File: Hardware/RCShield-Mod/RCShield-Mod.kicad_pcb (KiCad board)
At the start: 2 copper layers, 12 parts, among them K1 PPM_OUT, P1 ANALOG_EXT, P2 DIGI_EXT, P7 Vinput

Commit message: Changing VIA Size for the Analog Board Moving Analog Board away from Digital board connector
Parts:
- moved P1 9.40 mm to (109.0, 88.1)
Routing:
- net SCL: track 46.6 -> 55.9 mm
- net SDA: track 52.7 -> 59.9 mm
- net +5V: track 59.6 -> 57.0 mm
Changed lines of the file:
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@@
     (links 45)
     (no_connects 0)
-    (area 0 0 0 0)
+    (area 61.611934 74.676 167.640001 167.580733)
     (thickness 1.6)
     (drawings 0)
-    (tracks 123)
+    (tracks 121)
     (zones 0)
     (modules 12)
@@
   )
   (module PIN_ARRAY_4x1 (layer F.Cu)
-    (at 118.364 88.138)
+    (at 108.966 88.138)
     (descr "Double rangee de contacts 2 x 5 pins")
     (tags CONN)
@@
     )
   )
-  (segment (start 131.572 78.867) (end 136.779 78.867) (width 0.254) (layer F.Cu) (net 1))
-  (segment (start 114.554 86.106) (end 120.142 80.518) (width 0.254) (layer F.Cu) (net 1))
-  (segment (start 120.142 80.518) (end 138.43 80.518) (width 0.254) (layer F.Cu) (net 1))
-  (via (at 138.43 80.518) (size 2) (layers F.Cu B.Cu) (net 1))
-  (segment (start 114.554 86.106) (end 114.554 88.138) (width 0.254) (layer F.Cu) (net 1))
-  (segment (start 136.779 78.867) (end 138.43 80.518) (width 0.254) (layer F.Cu) (net 1))
+  (segment (start 131.572 78.867) (end 120.777 78.867) (width 0.254) (layer F.Cu) (net 1) (status 400000))
+  (segment (start 105.156 83.312) (end 109.474 78.994) (width 0.254) (layer F.Cu) (net 1))
+  (segment (start 109.474 78.994) (end 120.65 78.994) (width 0.254) (layer F.Cu) (net 1))
+  (via (at 120.65 78.994) (size 2) (layers F.Cu B.Cu) (net 1))
+  (segment (start 105.156 83.312) (end 105.156 88.138) (width 0.254) (layer F.Cu) (net 1) (status 800000))
+  (segment (start 120.777 78.867) (end 120.65 78.994) (width 0.254) (layer F.Cu) (net 1))
   (segment (start 145.288 88.138) (end 138.43 88.138) (width 0.254) (layer F.Cu) (net 1))
   (segment (start 138.303 88.265) (end 138.43 88.138) (width 0.254) (layer F.Cu) (net 1))
@@
   (segment (start 104.394 136.906) (end 108.204 136.906) (width 0.254) (layer B.Cu) (net 14))
   (segment (start 107.696 136.906) (end 108.204 136.906) (width 0.254) (layer B.Cu) (net 14))
-  (segment (start 131.572 82.169) (end 122.555 82.169) (width 0.254) (layer F.Cu) (net 15))
-  (segment (start 119.634 85.09) (end 119.634 88.138) (width 0.254) (layer F.Cu) (net 15))
-  (segment (start 122.555 82.169) (end 119.634 85.09) (width 0.254) (layer F.Cu) (net 15))
+  (segment (start 110.236 88.138) (end 110.236 85.344) (width 0.254) (layer F.Cu) (net 15) (status 400000))
+  (segment (start 113.411 82.169) (end 131.572 82.169) (width 0.254) (layer F.Cu) (net 15) (status 800000))
+  (segment (start 110.236 85.344) (end 113.411 82.169) (width 0.254) (layer F.Cu) (net 15))
   (segment (start 135.382 82.296) (end 131.699 82.296) (width 0.254) (layer F.Cu) (net 15))
   (segment (start 150.368 86.36) (end 146.304 82.296) (width 0.254) (layer F.Cu) (net 15))
@@
   (segment (start 131.699 82.296) (end 131.572 82.169) (width 0.254) (layer F.Cu) (net 15))
   (segment (start 150.368 96.266) (end 150.368 88.138) (width 0.254) (layer F.Cu) (net 15))
-  (segment (start 131.572 84.963) (end 129.667 84.963) (width 0.254) (layer F.Cu) (net 16))
-  (segment (start 117.094 90.17) (end 117.094 88.138) (width 0.254) (layer F.Cu) (net 16))
-  (segment (start 118.364 91.44) (end 117.094 90.17) (width 0.254) (layer F.Cu) (net 16))
-  (segment (start 124.968 91.44) (end 118.364 91.44) (width 0.254) (layer F.Cu) (net 16))
-  (segment (start 126.238 90.17) (end 124.968 91.44) (width 0.254) (layer F.Cu) (net 16))
-  (segment (start 126.238 88.392) (end 126.238 90.17) (width 0.254) (layer F.Cu) (net 16))
-  (segment (start 129.667 84.963) (end 126.238 88.392) (width 0.254) (layer F.Cu) (net 16))
+  (segment (start 107.696 88.138) (end 107.696 88.9) (width 0.254) (layer F.Cu) (net 16) (status C00000))
+  (segment (start 127.381 84.963) (end 131.572 84.963) (width 0.254) (layer F.Cu) (net 16) (status 800000))
+  (segment (start 121.412 90.932) (end 127.381 84.963) (width 0.254) (layer F.Cu) (net 16))
+  (segment (start 109.728 90.932) (end 121.412 90.932) (width 0.254) (layer F.Cu) (net 16))
+  (segment (start 107.696 88.9) (end 109.728 90.932) (width 0.254) (layer F.Cu) (net 16) (status 400000))
   (segment (start 135.382 84.836) (end 131.699 84.836) (width 0.254) (layer F.Cu) (net 16))
   (segment (start 147.828 86.36) (end 146.304 84.836) (width 0.254) (layer F.Cu) (net 16))
@@
   (via (at 94.996 123.952) (size 2) (layers F.Cu B.Cu) (net 17))
   (segment (start 97.536 126.492) (end 94.996 123.952) (width 0.254) (layer B.Cu) (net 17))
-  (segment (start 109.728 144.526) (end 109.728 136.144) (width 0.254) (layer F.Cu) (net 18) (status 400000))
-  (segment (start 77.343 128.143) (end 77.343 129.032) (width 0.254) (layer F.Cu) (net 18) (status C00000))
-  (segment (start 78.994 126.492) (end 77.343 128.143) (width 0.254) (layer F.Cu) (net 18) (status 800000))
+  (segment (start 109.728 144.526) (end 109.728 136.144) (width 0.254) (layer F.Cu) (net 18))
+  (segment (start 77.343 128.143) (end 77.343 129.032) (width 0.254) (layer F.Cu) (net 18))
+  (segment (start 78.994 126.492) (end 77.343 128.143) (width 0.254) (layer F.Cu) (net 18))
   (segment (start 100.076 126.492) (end 78.994 126.492) (width 0.254) (layer F.Cu) (net 18))
   (segment (start 109.728 136.144) (end 100.076 126.492) (width 0.254) (layer F.Cu) (net 18))
@@
   (segment (start 75.438 119.38) (end 77.343 121.285) (width 0.254) (layer F.Cu) (net 18))
   (segment (start 74.54392 129.032) (end 77.343 129.032) (width 0.254) (layer F.Cu) (net 18))
-  (segment (start 80.645 133.604) (end 80.645 140.589) (width 0.254) (layer F.Cu) (net 19) (status 400000))
-  (segment (start 122.428 151.13) (end 122.428 144.526) (width 0.254) (layer F.Cu) (net 19) (status 800000))
+  (segment (start 80.645 133.604) (end 80.645 140.589) (width 0.254) (layer F.Cu) (net 19))
+  (segment (start 122.428 151.13) (end 122.428 144.526) (width 0.254) (layer F.Cu) (net 19))
   (segment (start 120.904 152.654) (end 122.428 151.13) (width 0.254) (layer F.Cu) (net 19))
   (segment (start 92.71 152.654) (end 120.904 152.654) (width 0.254) (layer F.Cu) (net 19))

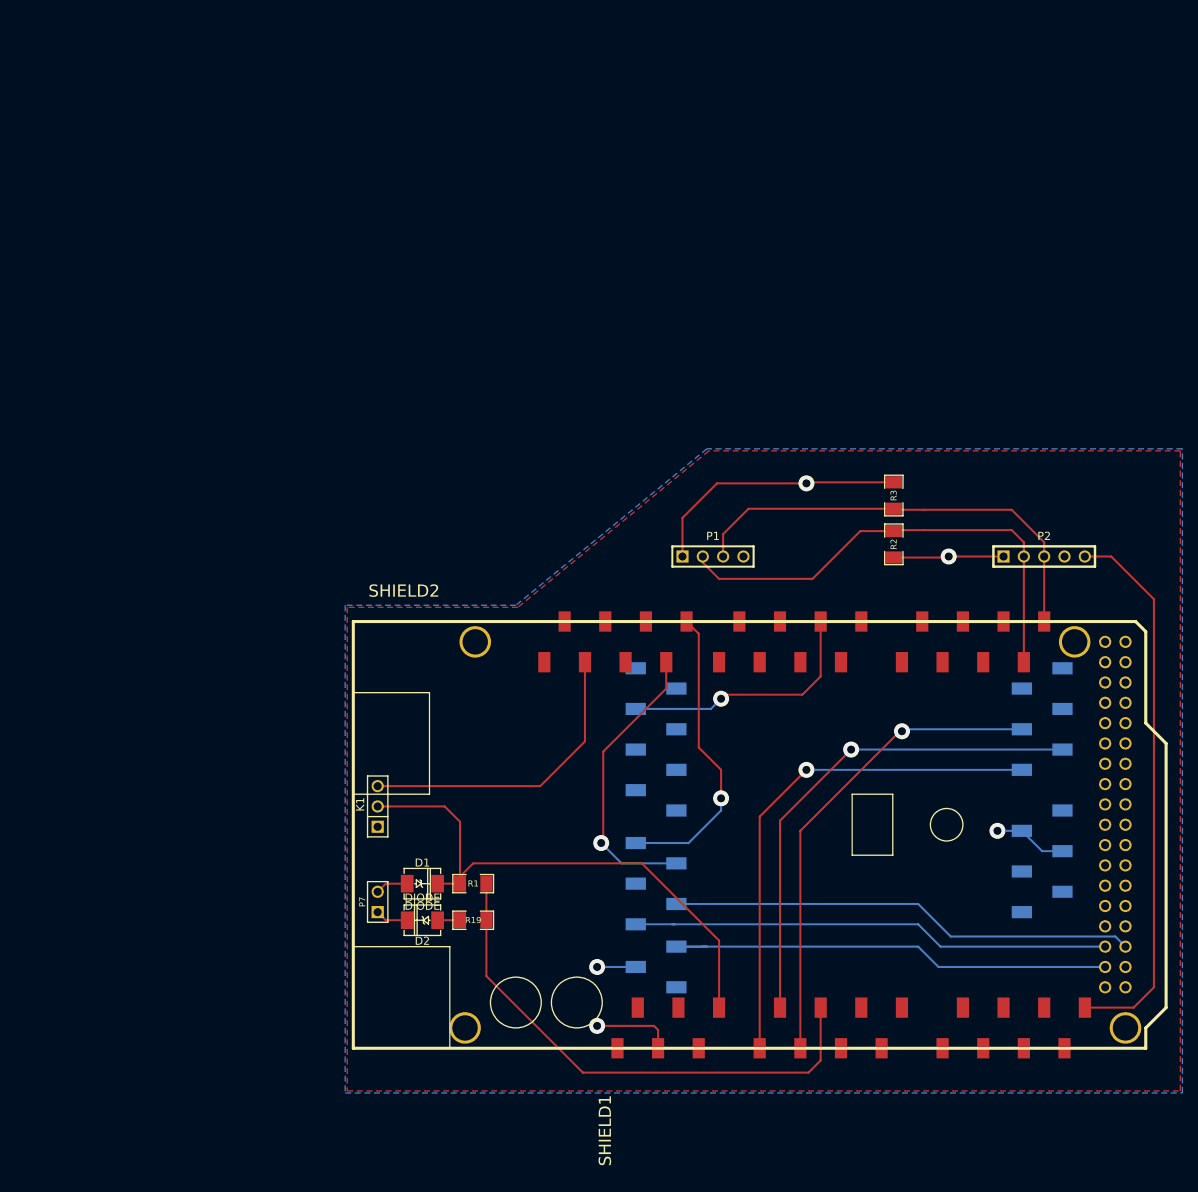
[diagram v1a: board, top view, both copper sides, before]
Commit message: Updated PCB to make it more DIY friendly Changed Vsense pin to A3 Added Design Folder
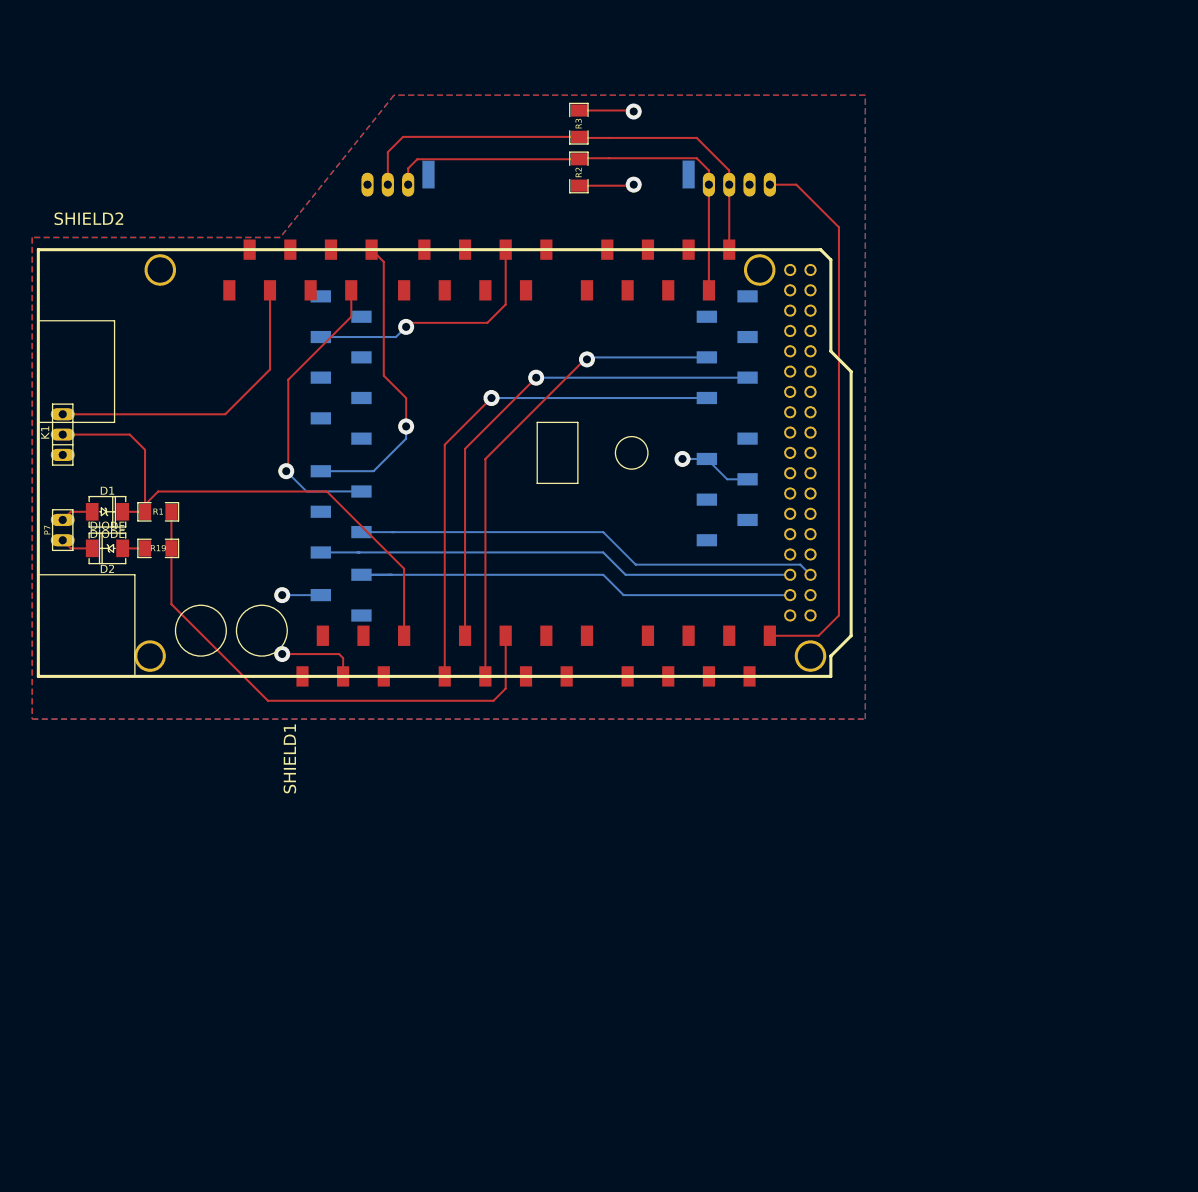
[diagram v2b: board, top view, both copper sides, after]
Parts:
- K1: footprint PIN_ARRAY_3X1 -> PIN_ARRAY_3X1_BIG
- P1: footprint PIN_ARRAY_4x1 -> PIN_ARRAY_4x1_MIXED2; moved to B.Cu
- P2: footprint PIN_ARRAY_5x1 -> PIN_ARRAY_5x1_MIXED3; moved to B.Cu
- P7: footprint PIN_ARRAY_2X1 -> PIN_ARRAY_2X1_BIG
- moved D1 60.9 mm to (33.3, 82.5)
- moved D2 60.9 mm to (33.3, 87.1)
- moved P7 60.9 mm to (27.7, 84.8)
- moved R1 60.9 mm to (39.6, 82.5)
- moved R19 60.9 mm to (39.6, 87.1)
- moved P1 60.9 mm to (69.6, 41.7), turned to 180 degrees
- moved P2 60.9 mm to (111.0, 41.7)
- moved R2 60.9 mm to (92.2, 40.1)
- moved R3 60.9 mm to (92.2, 34.0)
- moved K1 60.9 mm to (27.7, 72.9)
- moved SHIELD1 60.9 mm to (113.3, 119.1)
- moved SHIELD2 60.9 mm to (24.6, 103.1)
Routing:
- net +5V: track 57.0 -> 23.9 mm
- net SDA: track 59.9 -> 55.8 mm
- net SCL: track 55.9 -> 59.2 mm

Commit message: Adding Filter Cap to main board Adding ADC Channel re-map Disabling digital IO Configuration in preparation for the new breakout board.
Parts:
- added C1: 220uF, C1V5H, F.Cu at (39.1, 59.7)
- moved K1 2.54 mm to (27.7, 75.4)
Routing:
- net VIN: track 68.0 -> 63.1 mm
- net PPM: track 38.1 -> 38.9 mm
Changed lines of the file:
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@@
 (kicad_pcb (version 3) (host pcbnew "(2013-07-07 BZR 4022)-stable")
   (general
-    (links 45)
+    (links 47)
     (no_connects 0)
-    (area 22.241934 28.194 128.270001 121.098733)
+    (area 0 0 0 0)
     (thickness 1.6)
     (drawings 0)
     (tracks 115)
     (zones 0)
-    (modules 12)
+    (modules 13)
     (nets 20)
   )
@@
   (net 9 MISO)
   (net 10 MOSI)
-  (net 11 N-0000019)
-  (net 12 N-0000020)
+  (net 11 N-0000016)
+  (net 12 N-0000017)
   (net 13 PPM)
   (net 14 SCK)
@@
     (add_net MISO)
     (add_net MOSI)
-    (add_net N-0000019)
-    (add_net N-0000020)
+    (add_net N-0000016)
+    (add_net N-0000017)
     (add_net PPM)
     (add_net SCK)
@@
     (pad 1 smd rect (at -1.89992 0) (size 1.6002 2.19964)
       (layers F.Cu F.Paste F.Mask)
-      (net 11 N-0000019)
+      (net 11 N-0000016)
     )
     (pad 2 smd rect (at 1.89992 0) (size 1.6002 2.19964)
@@
     (pad 2 smd rect (at 1.89992 0 180) (size 1.6002 2.19964)
       (layers F.Cu F.Paste F.Mask)
-      (net 12 N-0000020)
+      (net 12 N-0000017)
     )
     (model smd/do214.wrl
@@
   )
   (module PIN_ARRAY_3X1_BIG (layer F.Cu)
-    (at 27.686 72.898 90)
+    (at 27.686 75.438 90)
     (descr "Connecteur 3 pins")
     (tags "CONN DEV")
@@
     (pad 1 thru_hole oval (at -1.27 0 90) (size 1.524 3) (drill 1.016)
       (layers *.Cu *.Mask F.SilkS)
-      (net 12 N-0000020)
+      (net 12 N-0000017)
     )
     (pad 2 thru_hole oval (at 1.27 0 90) (size 1.524 3) (drill 1.016)
       (layers *.Cu *.Mask F.SilkS)
-      (net 11 N-0000019)
+      (net 11 N-0000016)
     )
     (model pin_array/pins_array_2x1.wrl
@@
     )
     (model pin_array/pins_array_5x1.wrl
+      (at (xyz 0 0 0))
+      (scale (xyz 1 1 1))
+      (rotate (xyz 0 0 0))
+    )
+  )
+  (module C1V5H (layer F.Cu)
+    (at 39.116 59.69 270)
+    (descr "Condensateur e = 1 pas")
+    (tags C)
+    (fp_text reference C1 (at -1.27 7.62 360) (layer F.SilkS)
+      (effects (font (size 0.889 0.889) (thickness 0.127)))
+    )
+    (fp_text value 220uF (at 1.27 7.62 360) (layer F.SilkS)
+      (effects (font (size 0.889 0.889) (thickness 0.127)))
+    )
+    (fp_line (start -3.048 12.7) (end 3.048 12.7) (layer F.SilkS) (width 0.381))
+    (fp_line (start -3.048 1.27) (end 3.048 1.27) (layer F.SilkS) (width 0.381))
+    (fp_line (start -3.048 12.7) (end -3.048 1.27) (layer F.SilkS) (width 0.381))
+    (fp_line (start 3.048 1.27) (end 3.048 12.7) (layer F.SilkS) (width 0.381))
+    (fp_line (start -1.27 0) (end -1.27 1.27) (layer F.SilkS) (width 0.381))
+    (fp_line (start 1.27 0) (end 1.27 1.27) (layer F.SilkS) (width 0.381))
+    (fp_text user + (at -1.27 2.54 270) (layer F.SilkS)
+      (effects (font (size 0.762 0.762) (thickness 0.2032)))
+    )
+    (pad 1 thru_hole rect (at -1.27 0 270) (size 1.397 1.397) (drill 0.8128)
+      (layers *.Cu *.Mask F.SilkS)
+      (net 1 +5V)
+    )
+    (pad 2 thru_hole circle (at 1.27 0 270) (size 1.397 1.397) (drill 0.8128)
+      (layers *.Cu *.Mask F.SilkS)
+      (net 7 GND)
+    )
+    (model discret/c_horiz_c1v5.wrl
       (at (xyz 0 0 0))
       (scale (xyz 1 1 1))
@@
   (segment (start 31.37408 87.122) (end 28.702 87.122) (width 0.254) (layer F.Cu) (net 12))
   (segment (start 28.702 87.122) (end 27.686 86.106) (width 0.254) (layer F.Cu) (net 12))
-  (segment (start 53.594 54.864) (end 53.594 64.77) (width 0.254) (layer F.Cu) (net 13))
-  (segment (start 48.006 70.358) (end 27.686 70.358) (width 0.254) (layer F.Cu) (net 13))
-  (segment (start 53.594 64.77) (end 48.006 70.358) (width 0.254) (layer F.Cu) (net 13))
+  (segment (start 27.686 72.898) (end 44.958 72.898) (width 0.254) (layer F.Cu) (net 13) (status 400000))
+  (segment (start 53.594 64.262) (end 53.594 54.864) (width 0.254) (layer F.Cu) (net 13) (status 800000))
+  (segment (start 44.958 72.898) (end 53.594 64.262) (width 0.254) (layer F.Cu) (net 13))
   (segment (start 65.024 90.424) (end 95.25 90.424) (width 0.254) (layer B.Cu) (net 14))
   (segment (start 97.79 92.964) (end 118.618 92.964) (width 0.254) (layer B.Cu) (net 14))
@@
   (segment (start 65.024 80.01) (end 58.166 80.01) (width 0.254) (layer B.Cu) (net 17))
   (segment (start 58.166 80.01) (end 55.626 77.47) (width 0.254) (layer B.Cu) (net 17))
+  (segment (start 27.686 75.438) (end 35.306 75.438) (width 0.254) (layer F.Cu) (net 18) (status 400000))
+  (segment (start 39.624 79.756) (end 39.624 80.01) (width 0.254) (layer F.Cu) (net 18))
+  (segment (start 35.306 75.438) (end 39.624 79.756) (width 0.254) (layer F.Cu) (net 18))
   (segment (start 70.358 98.044) (end 70.358 89.662) (width 0.254) (layer F.Cu) (net 18))
   (segment (start 37.973 81.661) (end 37.973 82.55) (width 0.254) (layer F.Cu) (net 18))
@@
   (segment (start 60.706 80.01) (end 39.624 80.01) (width 0.254) (layer F.Cu) (net 18))
   (segment (start 70.358 89.662) (end 60.706 80.01) (width 0.254) (layer F.Cu) (net 18))
-  (segment (start 27.686 72.898) (end 36.068 72.898) (width 0.254) (layer F.Cu) (net 18))
-  (segment (start 37.973 74.803) (end 37.973 82.55) (width 0.254) (layer F.Cu) (net 18))
-  (segment (start 36.068 72.898) (end 37.973 74.803) (width 0.254) (layer F.Cu) (net 18))
   (segment (start 35.17392 82.55) (end 37.973 82.55) (width 0.254) (layer F.Cu) (net 18))
   (segment (start 41.275 87.122) (end 41.275 94.107) (width 0.254) (layer F.Cu) (net 19))
